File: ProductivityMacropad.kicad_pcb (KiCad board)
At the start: 2 copper layers, 15 parts, among them SW1 SW_Push, SW2 SW_Push, SW3 SW_Push, SW4 SW_Push, SW5 SW_Push, SW6 SW_Push, SW7 SW_Push, SW8 RotaryEncoder

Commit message: Updated PCB
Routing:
- net Net-(D3-A): track 9.14 -> 0.00 mm
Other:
- board outline added: 110 x 60.2 mm
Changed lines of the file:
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@@
 		)
+	)
+	(gr_rect
+		(start 70 70)
+		(end 180 130.16)
+		(stroke
+			(width 0.05)
+			(type default)
+		)
+		(fill no)
+		(layer "Edge.Cuts")
 	)
 	(segment
@@
 		(net 32)
 	)
-	(segment
-		(start 134.84 79.46)
-		(end 134.84 77.62)
-		(width 0.2)
-		(layer "B.Cu")
-		(net 33)
-	)
-	(segment
-		(start 134.84 77.62)
-		(end 140 72.46)
-		(width 0.2)
-		(layer "B.Cu")
-		(net 33)
-	)
 	(embedded_fonts no)

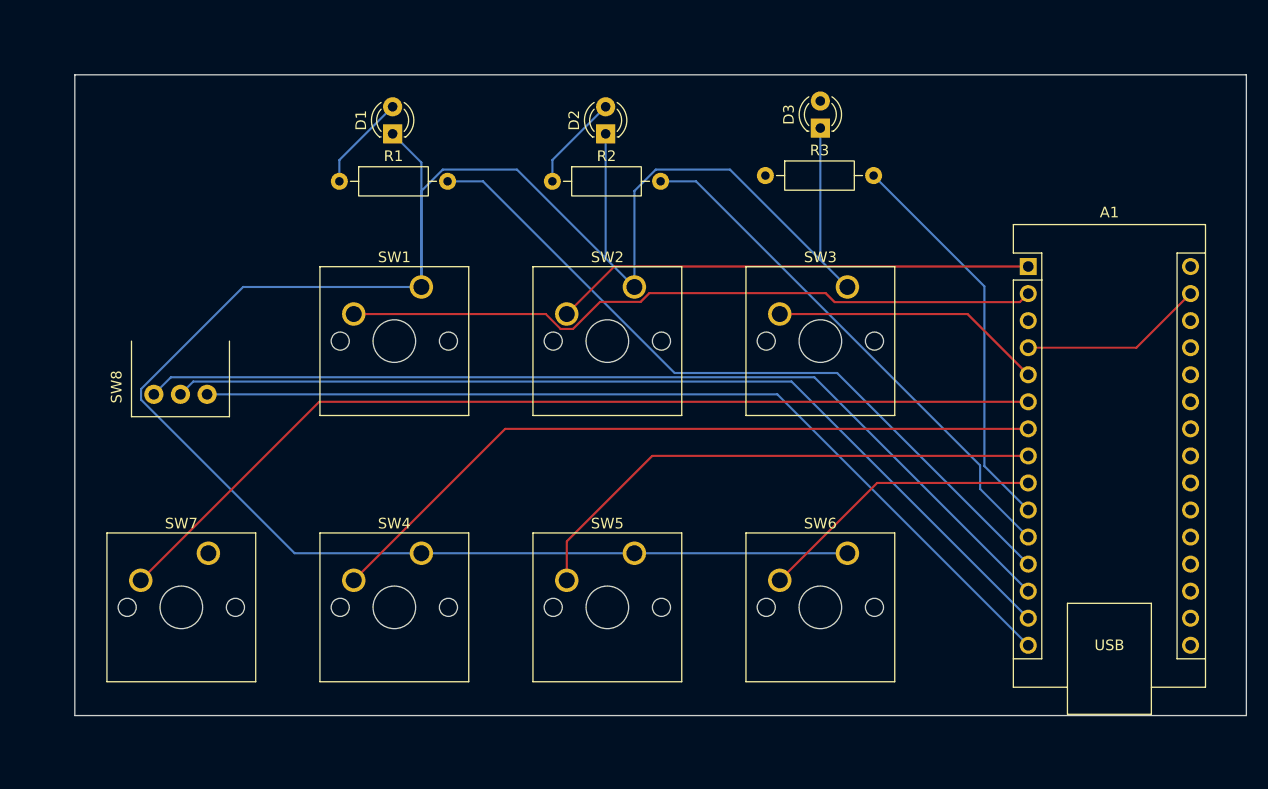
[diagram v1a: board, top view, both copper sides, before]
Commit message: Updated faulty PCB (again)
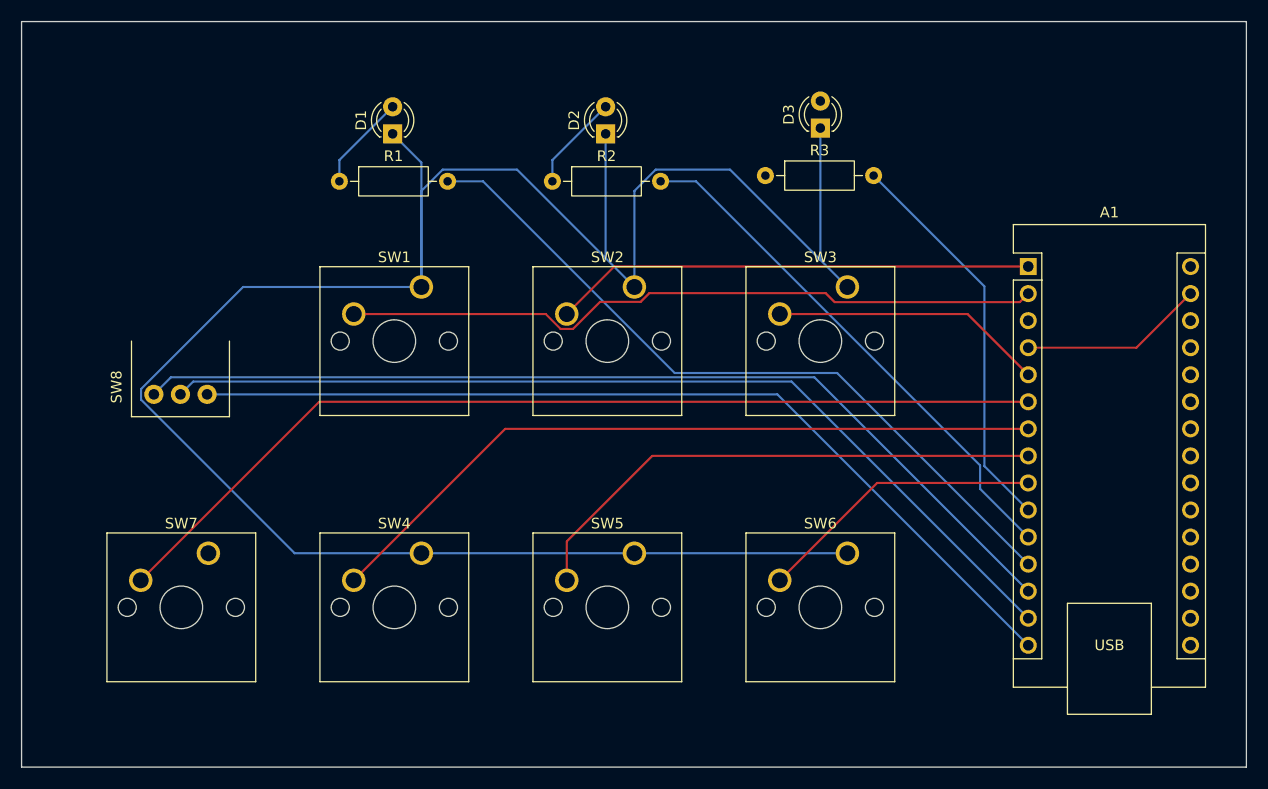
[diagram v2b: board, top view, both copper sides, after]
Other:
- board size 110 x 60.2 mm -> 115 x 70 mm
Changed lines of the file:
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@@
 	)
 	(gr_rect
-		(start 70 70)
-		(end 180 130.16)
+		(start 65 65)
+		(end 180 135)
 		(stroke
 			(width 0.05)
